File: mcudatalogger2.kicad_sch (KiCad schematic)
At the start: 1 part

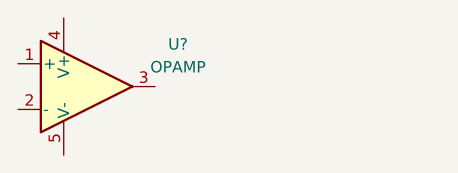
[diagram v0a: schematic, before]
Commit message: added a second opamp
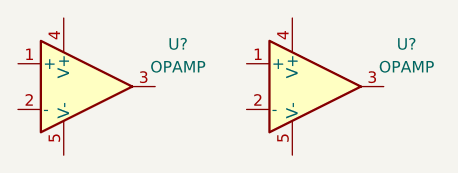
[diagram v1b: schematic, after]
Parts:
- added U?: OPAMP, symbol pspice:OPAMP
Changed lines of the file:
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@@
 (kicad_sch (version 20211123) (generator eeschema)
   (paper "A4")
+  (symbol (lib_id "pspice:OPAMP") (at 171.45 80.01 0) (unit 1)
+    (in_bom yes) (on_board yes) (fields_autoplaced)
+    (property "Reference" "U?" (id 0) (at 181.61 75.311 0))
+    (property "Value" "OPAMP" (id 1) (at 181.61 77.851 0))
+    (property "Footprint" "" (id 2) (at 171.45 80.01 0)
+      (effects (font (size 1.27 1.27)) hide)
+    )
+    (property "Datasheet" "~" (id 3) (at 171.45 80.01 0)
+      (effects (font (size 1.27 1.27)) hide)
+    )
+    (pin "1")
+    (pin "2")
+    (pin "3")
+    (pin "4")
+    (pin "5")
+  )
   (symbol (lib_id "pspice:OPAMP") (at 146.05 80.01 0) (unit 1)
     (in_bom yes) (on_board yes) (fields_autoplaced)
@@
   )
   (symbol_instances
+    (path "/54b0844f-3a07-47b5-8f74-83a0fc1a210a"
+      (reference "U?") (unit 1) (value "OPAMP") (footprint "")
+    )
     (path "/d951a515-2cce-4abd-bf2b-30db4286398f"
       (reference "U?") (unit 1) (value "OPAMP") (footprint "")

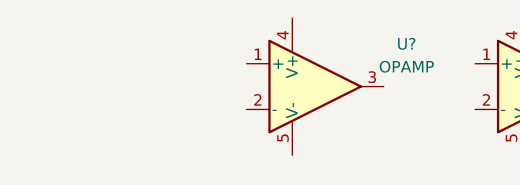
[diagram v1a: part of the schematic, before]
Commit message: added a third opamp but in experimental
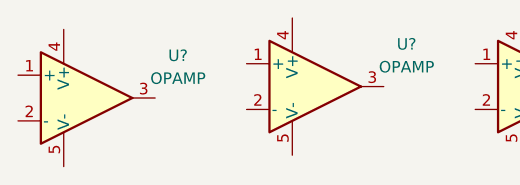
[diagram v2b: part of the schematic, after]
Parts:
- added U?: OPAMP, symbol pspice:OPAMP
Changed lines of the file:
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@@
 (kicad_sch (version 20211123) (generator eeschema)
   (paper "A4")
+  (symbol (lib_id "pspice:OPAMP") (at 120.65 81.28 0) (unit 1)
+    (in_bom yes) (on_board yes) (fields_autoplaced)
+    (property "Reference" "U?" (id 0) (at 130.81 76.581 0))
+    (property "Value" "OPAMP" (id 1) (at 130.81 79.121 0))
+    (property "Footprint" "" (id 2) (at 120.65 81.28 0)
+      (effects (font (size 1.27 1.27)) hide)
+    )
+    (property "Datasheet" "~" (id 3) (at 120.65 81.28 0)
+      (effects (font (size 1.27 1.27)) hide)
+    )
+    (pin "1")
+    (pin "2")
+    (pin "3")
+    (pin "4")
+    (pin "5")
+  )
   (symbol (lib_id "pspice:OPAMP") (at 171.45 80.01 0) (unit 1)
     (in_bom yes) (on_board yes) (fields_autoplaced)
@@
   )
   (symbol_instances
+    (path "/33c06d8b-305c-476e-8f99-f7a5ff73f6f9"
+      (reference "U?") (unit 1) (value "OPAMP") (footprint "")
+    )
     (path "/54b0844f-3a07-47b5-8f74-83a0fc1a210a"
       (reference "U?") (unit 1) (value "OPAMP") (footprint "")

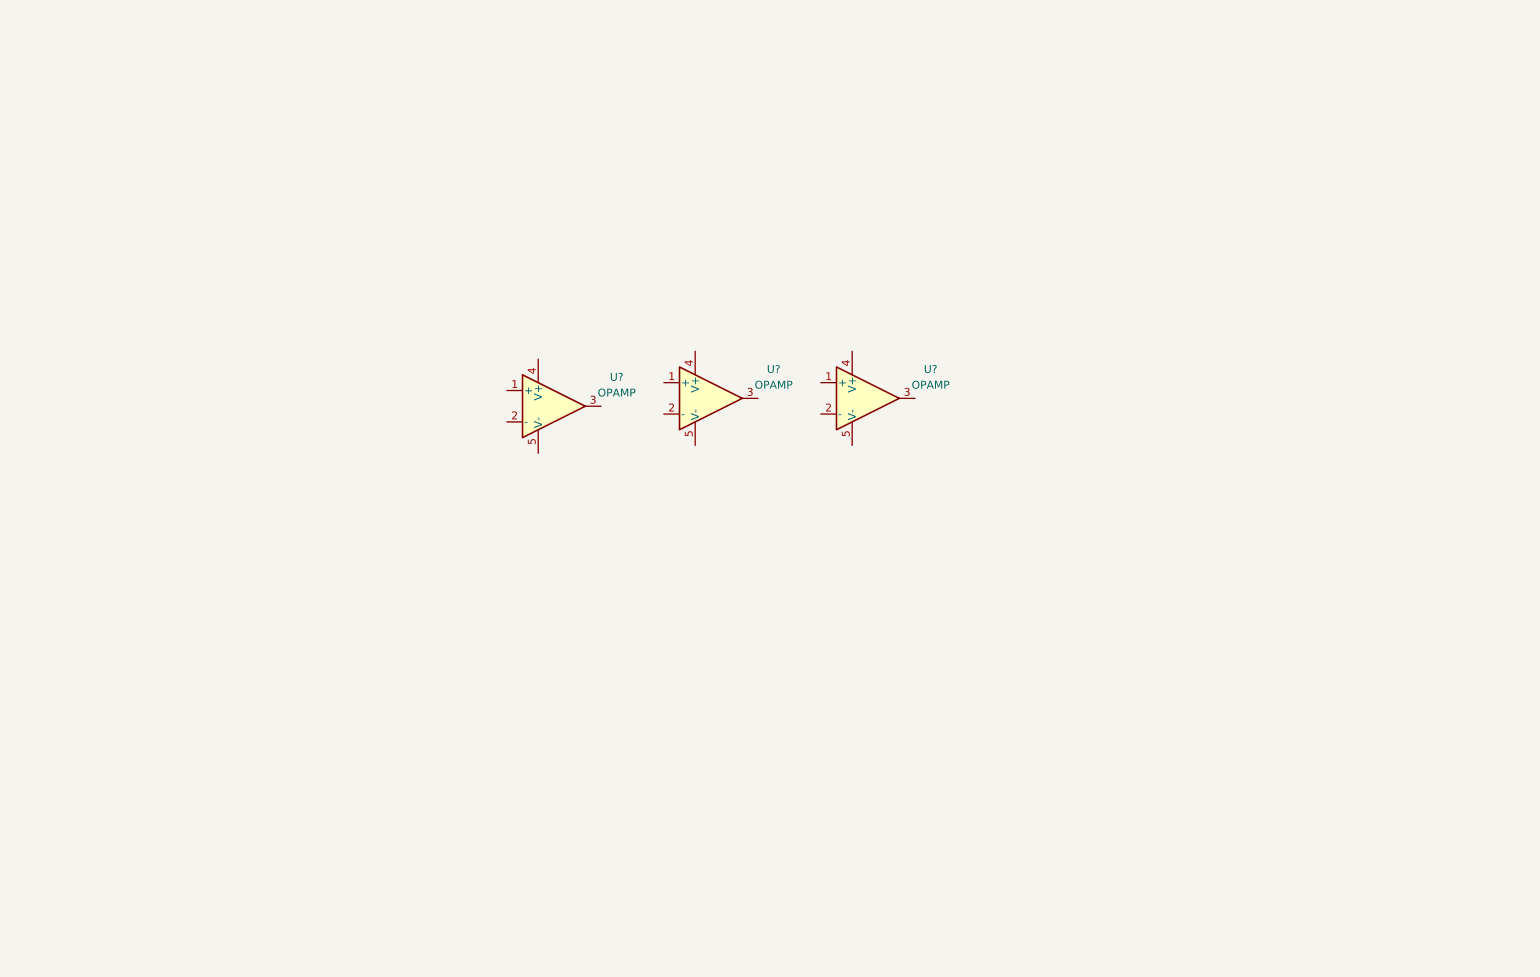
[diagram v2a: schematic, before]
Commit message: laid out all the elements
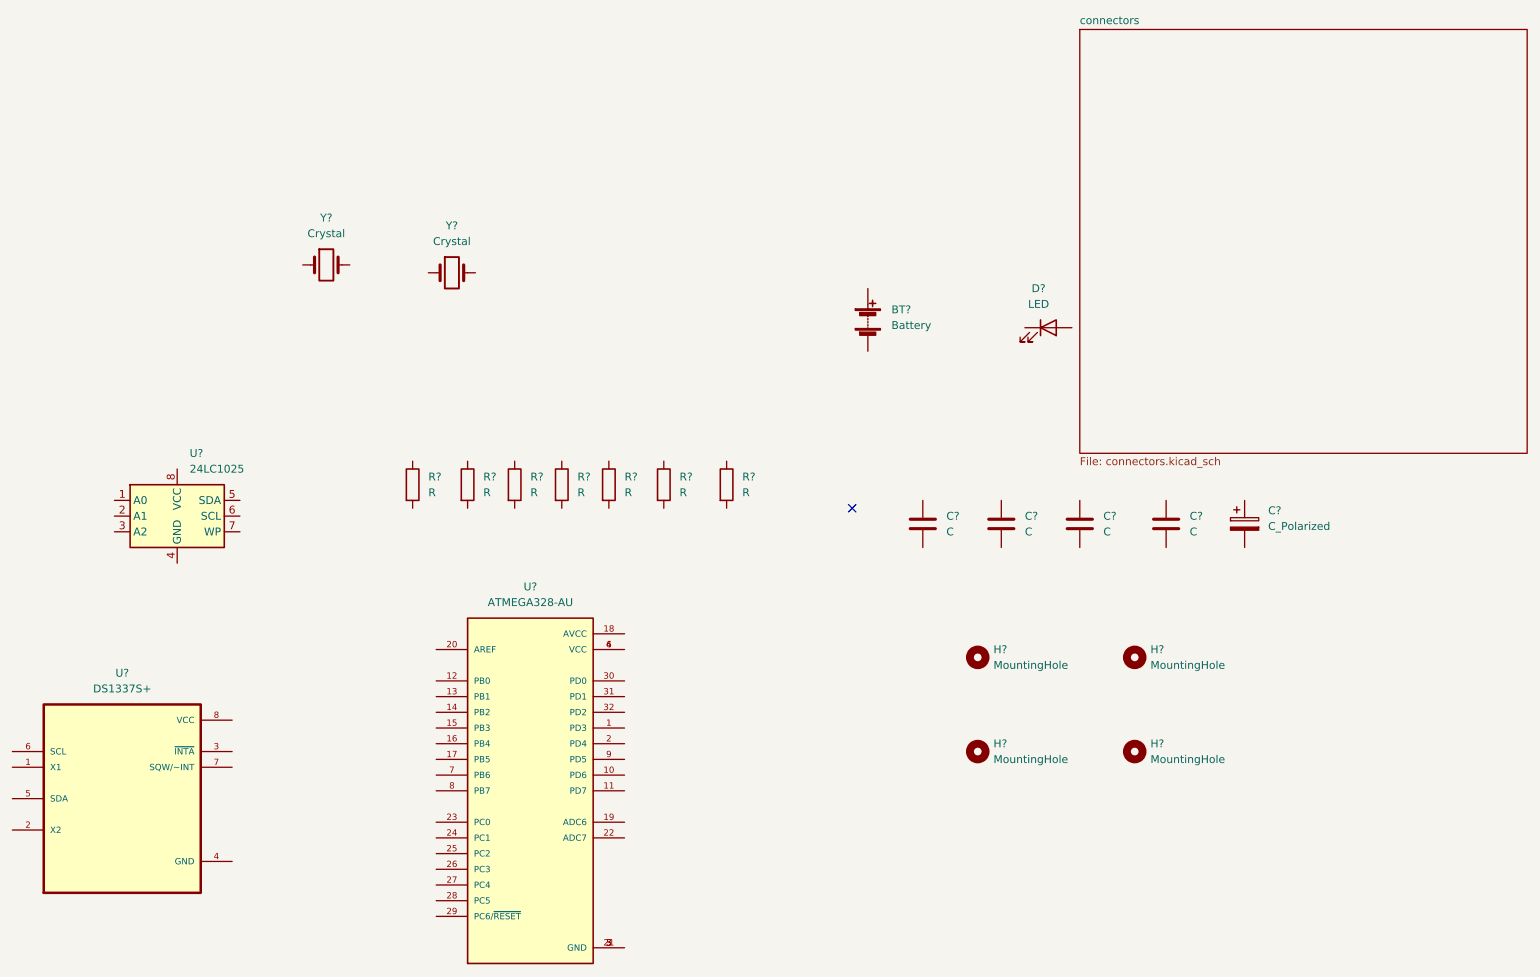
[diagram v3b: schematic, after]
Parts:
- removed U? (x3): OPAMP, symbol pspice:OPAMP
- added BT?: Battery, symbol Device:Battery
- added C? (x4): C, symbol Device:C
- added C?: C_Polarized, symbol Device:C_Polarized
- added D?: LED, symbol Device:LED
- added H? (x4): MountingHole, symbol Mechanical:MountingHole
- added R? (x7): R, symbol Device:R
- added U?: 24LC1025, symbol Memory_EEPROM:24LC1025
- added U?: DS1337S+, SOIC127P600X175-8N, symbol DS1337S_:DS1337S+
- added U?: ATMEGA328-AU, QFP80P900X900X120-32N, symbol ATMEGA328-AU:ATMEGA328-AU
- added Y? (x2): Crystal, symbol Device:Crystal
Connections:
- new net: U?.21 (GND), U?.3 (GND), U?.5 (GND)
- new net: U?.4 (VCC), U?.6 (VCC)
- no-connect marks 0 -> 1
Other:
- added sheet connectors (connectors.kicad_sch)
